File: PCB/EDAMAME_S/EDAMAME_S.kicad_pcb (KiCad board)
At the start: 2 copper layers, 80 x 87 mm, 62 parts, among them CN1 USB-B-MICRO, J1 Conn_01x20, J2 Conn_01x20, J5 Nichrome, M1 Motor_L, M2 Motor_R, Q1 2N7002DW, Q2 FDS4675, Q3 2SC2712, SW1 power, SW2 RST, U1 microSD, U2 FT231XS, U3 ESP32-WROOM, U4 TPS63000, U5 LSM303C, U6 GYSFDMAXB, U7 BD6211F, U8 INA226, U9 BD6211F

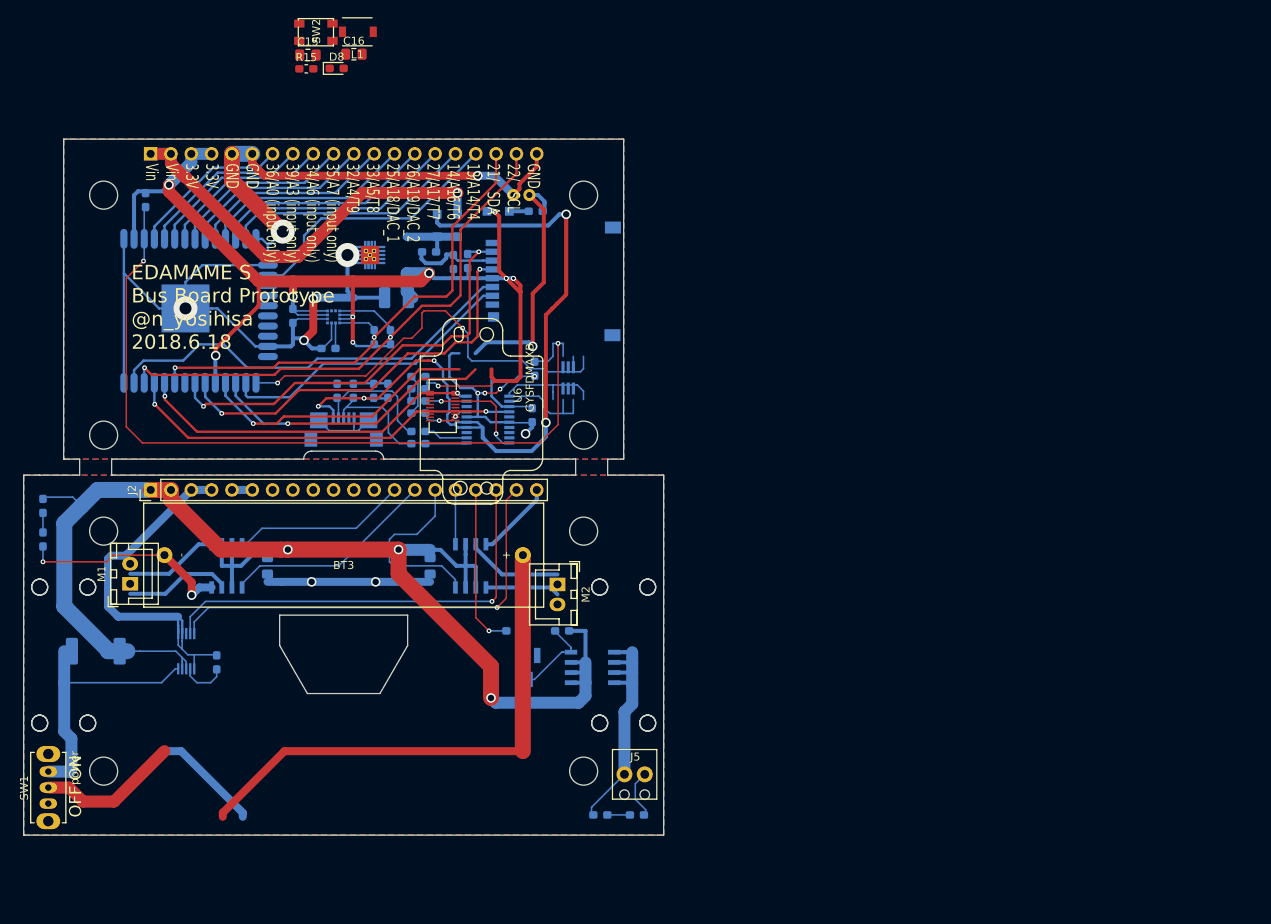
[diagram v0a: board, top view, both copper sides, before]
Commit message: AVR フットプリント・基板外形割当
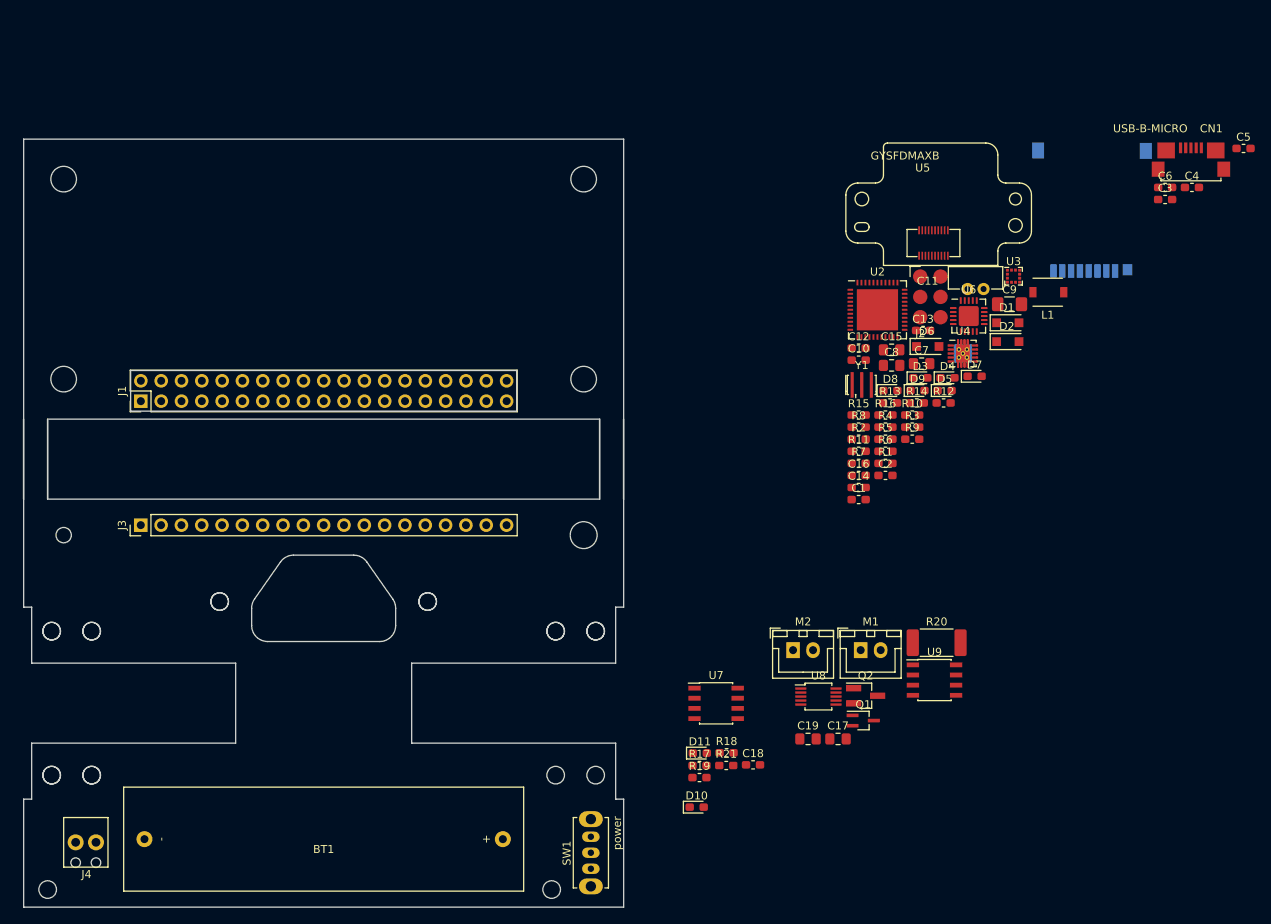
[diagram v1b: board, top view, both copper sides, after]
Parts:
- removed BT3: 10440, user:BH-411
- removed J5: Nichrome, user:MPT0.5_2-2.54
- removed Q3: 2SC2712, Package_TO_SOT_SMD:SOT-23_Handsoldering
- removed SW2: RST, user:SKRPACE010_kai
- added C17: 10u, Capacitor_SMD:C_0805_2012Metric_Pad1.15x1.40mm_HandSolder, F.Cu at (130.3, 92.1)
- added C18: 0.1u, Capacitor_SMD:C_0603_1608Metric_Pad1.05x0.95mm_HandSolder, F.Cu at (119.7, 95.4)
- added C19: 10u, Capacitor_SMD:C_0805_2012Metric_Pad1.15x1.40mm_HandSolder, F.Cu at (126.6, 92.1)
- added D10: Nichrome, LED_SMD:LED_0603_1608Metric_Pad1.05x0.95mm_HandSolder, F.Cu at (112.7, 100.7)
- added D11: POWER, LED_SMD:LED_0603_1608Metric_Pad1.05x0.95mm_HandSolder, F.Cu at (113.1, 93.9)
- added D9: RX_LED, LED_SMD:LED_0603_1608Metric_Pad1.05x0.95mm_HandSolder, F.Cu at (140.3, 48.6)
- added J3: Conn, Connector_PinHeader_2.54mm:PinHeader_1x19_P2.54mm_Vertical, F.Cu at (43.2, 65.4)
- added J4: Nichrome, user:MPT0.5_2-2.54, F.Cu at (33.6, 108.2)
- added R16: 1k, Resistor_SMD:R_0603_1608Metric_Pad1.05x0.95mm_HandSolder, F.Cu at (136.3, 51.6)
- added R17: 10K, Resistor_SMD:R_0603_1608Metric_Pad1.05x0.95mm_HandSolder, F.Cu at (113.0, 95.5)
- added R18: 1K, Resistor_SMD:R_0603_1608Metric_Pad1.05x0.95mm_HandSolder, F.Cu at (116.4, 93.9)
- added R19: 10K, Resistor_SMD:R_0603_1608Metric_Pad1.05x0.95mm_HandSolder, F.Cu at (113.0, 97.0)
- added R20: 10m, Resistor_SMD:R_2512_6332Metric_Pad1.52x3.35mm_HandSolder, F.Cu at (142.7, 80.1)
- added R21: 1K, Resistor_SMD:R_0603_1608Metric_Pad1.05x0.95mm_HandSolder, F.Cu at (116.4, 95.5)
- added Y1: 16MHz, Crystal:Resonator_SMD_muRata_CSTxExxV-3Pin_3.0x1.1mm_HandSoldering, F.Cu at (133.3, 47.9)
- BT1: value BACKUP -> 10440; footprint user:MS621FE_FL11E -> user:BH-411; moved to F.Cu
- C1, C12, C2, C5, CN1: moved to F.Cu
- C10: value 100u -> 0.1u; footprint Capacitor_SMD:C_1210_3225Metric_Pad1.42x2.65mm_HandSolder -> Capacitor_SMD:C_0603_1608Metric_Pad1.05x0.95mm_HandSolder; moved to F.Cu
- C11: value 10u -> 0.22F 3.3V; footprint Capacitor_SMD:C_0805_2012Metric_Pad1.15x1.40mm_HandSolder -> user:MS621FE_FL11E; moved to F.Cu
- C13: value 10u -> 47p; footprint Capacitor_SMD:C_0805_2012Metric_Pad1.15x1.40mm_HandSolder -> Capacitor_SMD:C_0603_1608Metric_Pad1.05x0.95mm_HandSolder; moved to F.Cu
- C14: value 0.1u -> 47p; moved to F.Cu
- C16: value 10u -> 0.1u; footprint Capacitor_SMD:C_0805_2012Metric_Pad1.15x1.40mm_HandSolder -> Capacitor_SMD:C_0603_1608Metric_Pad1.05x0.95mm_HandSolder
- C3, C4: value 47p -> 0.1u; moved to F.Cu
- C6: value 10u -> 0.1u; moved to F.Cu
- C7, C8: value 0.1u -> 10u; footprint Capacitor_SMD:C_0603_1608Metric_Pad1.05x0.95mm_HandSolder -> Capacitor_SMD:C_0805_2012Metric_Pad1.15x1.40mm_HandSolder; moved to F.Cu
- C9: value 0.1u -> 100u; footprint Capacitor_SMD:C_0603_1608Metric_Pad1.05x0.95mm_HandSolder -> Capacitor_SMD:C_1206_3216Metric_Pad1.42x1.75mm_HandSolder; moved to F.Cu
- D1: value TXLED -> GS1010FL; footprint LED_SMD:LED_0603_1608Metric_Pad1.05x0.95mm_HandSolder -> Diode_SMD:D_SOD-123F; moved to F.Cu
- D2: value RXLED -> GS1010FL; footprint LED_SMD:LED_0603_1608Metric_Pad1.05x0.95mm_HandSolder -> Diode_SMD:D_SOD-123F; moved to F.Cu
- D3: value GS1010FL -> POWER; footprint Diode_SMD:D_SOD-123F -> LED_SMD:LED_0603_1608Metric_Pad1.05x0.95mm_HandSolder; moved to F.Cu
- D4: value GS1010FL -> LED1; footprint Diode_SMD:D_SOD-123F -> LED_SMD:LED_0603_1608Metric_Pad1.05x0.95mm_HandSolder; moved to F.Cu
- D5: value GS1010FL -> LED2; footprint Diode_SMD:D_SOD-123F -> LED_SMD:LED_0603_1608Metric_Pad1.05x0.95mm_HandSolder; moved to F.Cu
- D6: value Nichrome -> GS1010FL; footprint LED_SMD:LED_0603_1608Metric_Pad1.05x0.95mm_HandSolder -> Diode_SMD:D_SOD-123F; moved to F.Cu
- D7: value POWER -> 1PPS; moved to F.Cu
- D8: value GPS -> TX_LED
- J1: value Conn_01x20 -> Conn; footprint Connector_PinHeader_2.54mm:PinHeader_1x20_P2.54mm_Vertical -> Connector_PinHeader_2.54mm:PinHeader_2x19_P2.54mm_Vertical; moved to F.Cu
- J2: value Conn_01x20 -> ISP; footprint Connector_PinHeader_2.54mm:PinHeader_1x20_P2.54mm_Vertical -> user:AVR_ISP
- L1: value 2.2uH VLF4012-2R2 -> 2.2uH
- Q1: value 2N7002DW -> MTM231102LBF; footprint Package_TO_SOT_SMD:SOT-363_SC-70-6_Handsoldering -> Package_TO_SOT_SMD:SOT-323_SC-70_Handsoldering; moved to F.Cu
- Q2: value FDS4675 -> 2SC2712; footprint Package_SO:SOIC-8_3.9x4.9mm_P1.27mm -> Package_TO_SOT_SMD:SOT-23_Handsoldering; moved to F.Cu
- R1: value 10K -> 10k; moved to F.Cu
- R10: value 1K -> 1k; moved to F.Cu
- R11: value 10K -> 100; moved to F.Cu
- R12: value 10m -> 1k; footprint Resistor_SMD:R_2512_6332Metric_Pad1.52x3.35mm_HandSolder -> Resistor_SMD:R_0603_1608Metric_Pad1.05x0.95mm_HandSolder; moved to F.Cu
- R13: value 1K -> 33; moved to F.Cu
- R14: value 10K -> 33; moved to F.Cu
- R15: value 1K -> 1k
- R2, R3: value 33 -> 10k; moved to F.Cu
- R4, R5: value 1K -> 10k; moved to F.Cu
- R6, R7: value 2.2K -> 2.2k; moved to F.Cu
- R8: value 100 -> 1k; moved to F.Cu
- R9: value 10K -> 1k; moved to F.Cu
- U2: value FT231XS -> ATMEGA1284P-MU; footprint user:FT231XS -> Package_DFN_QFN:QFN-44-1EP_7x7mm_P0.5mm_EP5.15x5.15mm; moved to F.Cu
- U3: value ESP32-WROOM -> LSM303C; footprint ESP32-footprints-Lib:ESP32-WROOM -> Package_LGA:LGA-12_2x2mm_P0.5mm; moved to F.Cu
- U4: value TPS63000 -> TPS63001; moved to F.Cu
- U5: value LSM303C -> GYSFDMAXB; footprint Housings_LGA:LGA-12_2x2mm_Pitch0.5mm -> user:GYSFDMAXB; moved to F.Cu
- U6: value GYSFDMAXB -> FT231XQ; footprint user:GYSFDMAXB -> Package_DFN_QFN:QFN-20-1EP_4x4mm_P0.5mm_EP2.5x2.5mm
- U7, U9: footprint Housings_SOIC:SOIC-8_3.9x4.9mm_Pitch1.27mm -> Package_SO:SOIC-8_3.9x4.9mm_P1.27mm; moved to F.Cu
- U8: footprint Housings_SSOP:MSOP-10_3x3mm_Pitch0.5mm -> Package_SO:MSOP-10_3x3mm_P0.5mm; moved to F.Cu
- moved D7 118.2 mm to (147.4, 46.8), turned to 0 degrees
- moved C5 112.9 mm to (181.0, 18.3), turned to 0 degrees
- moved CN1 111.2 mm to (174.5, 20.9), turned to 0 degrees
- moved R12 110.4 mm to (143.5, 50.1), turned to 0 degrees
- moved C4 109.8 mm to (174.6, 23.2), turned to 0 degrees
- moved R13 106.7 mm to (136.8, 50.1), turned to 0 degrees
- moved U3 106.0 mm to (152.3, 34.3), turned to 0 degrees
- moved C3 104.3 mm to (171.2, 24.7), turned to 0 degrees
- moved C6 100.4 mm to (171.2, 23.2), turned to 0 degrees
- moved J2 99.8 mm to (140.6, 34.3), turned to 0 degrees
- moved R14 99.7 mm to (140.2, 50.1), turned to 0 degrees
- moved L1 92.2 mm to (156.6, 36.3)
- moved M1 91.7 mm to (133.2, 81.0), turned to 0 degrees
- moved C12 89.3 mm to (132.9, 43.3), turned to 0 degrees
- moved C13 87.1 mm to (141.0, 41.1), turned to 0 degrees
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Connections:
- BT1 pad 2: GND -> GNDPWR
- C11 pad 1: +BATT -> Net-(C11-Pad1)
- C11 pad 2: GNDPWR -> GND
- C12 pad 1: VCC -> Net-(C12-Pad1)
- C12 pad 2: GNDPWR -> /EDAMAME_S_core/RST
- C13 pad 1: +BATT -> Net-(C13-Pad1)
- C13 pad 2: GNDPWR -> GND
- C14 pad 1: /EN -> Net-(C13-Pad1)
- C15 pad 1: Net-(C15-Pad1) -> +5V
- C16 pad 1: +3V3 -> +5V
- C3 pad 1: Net-(C3-Pad1) -> +3V3
- C4 pad 1: Net-(C4-Pad1) -> +3V3
- C5 pad 1: +5V -> +3V3
- C6 pad 1: +5V -> Net-(C6-Pad1)
- C7 pad 1: +3V3 -> Net-(C7-Pad1)
- C8 pad 1: Net-(C8-Pad1) -> +3V3
- C9 pad 1: Net-(C15-Pad1) -> +3V3
- CN1 pad 2: Net-(C4-Pad1) -> Net-(C13-Pad1)
- CN1 pad 3: Net-(C3-Pad1) -> Net-(CN1-Pad3)
- D1 pad 1: Net-(D1-Pad1) -> Net-(C7-Pad1)
- D2 pad 1: Net-(D2-Pad1) -> Net-(C7-Pad1)
- D2 pad 2: Net-(D2-Pad2) -> +5V
- D3 pad 1: Net-(C15-Pad1) -> GND
- D3 pad 2: +5V -> Net-(D3-Pad2)
- D4 pad 1: Net-(C15-Pad1) -> GND
- D4 pad 2: VDC -> Net-(D4-Pad2)
- D5 pad 1: Net-(D5-Pad1) -> GND
- D5 pad 2: +3V3 -> Net-(D5-Pad2)
- D6 pad 1: GNDPWR -> Net-(C11-Pad1)
- D7 pad 1: GNDPWR -> GND
- D8 pad 1: GND -> Net-(D8-Pad1)
- J1 pad 1: VDC -> Net-(J1-Pad1)
- J1 pad 10: /IO35 -> /EDAMAME_S_core/18
- J1 pad 11: /IO32 -> /EDAMAME_S_core/1
- J1 pad 12: /IO33 -> /EDAMAME_S_core/19
- J1 pad 13: /IO25 -> /EDAMAME_S_core/2
- J1 pad 14: /IO26 -> /EDAMAME_S_core/20
- J1 pad 15: /IO27 -> /EDAMAME_S_core/3-
- J1 pad 16: /IO14 -> /EDAMAME_S_core/21
- J1 pad 17: /IO13 -> /EDAMAME_S_core/PC→AVR
- J1 pad 18: /I2C_SDA -> /EDAMAME_S_core/22
- J1 pad 19: /I2C_SCL -> /EDAMAME_S_core/AVR→PC
- J1 pad 2: VDC -> Net-(D1-Pad2)
- J1 pad 20: GND -> /EDAMAME_S_core/23
- J1 pad 3: +3V3 -> Net-(J1-Pad1)
- J1 pad 4: +3V3 -> Net-(D1-Pad2)
- J1 pad 5: GND -> +3V3
- J1 pad 6: GND -> +3V3
- J1 pad 7: /S_VP -> GND
- J1 pad 8: /S_VN -> GND
- J1 pad 9: /IO34 -> /EDAMAME_S_core/0
- J2 pad 1: +BATT -> /EDAMAME_S_core/MISO
- J2 pad 2: +BATT -> +3V3
- J2 pad 3: VCC -> /EDAMAME_S_core/SCK
- J2 pad 4: VCC -> /EDAMAME_S_core/MOSI
- J2 pad 5: GNDPWR -> /EDAMAME_S_core/RST
- J2 pad 6: GNDPWR -> GND
- Q1 pad 1: /RST -> Net-(Q1-Pad1)
- Q1 pad 2: /DTR -> Net-(J4-Pad1)
- Q1 pad 3: /BOOT -> +BATT
- Q2 pad 1: +BATT -> Net-(Q2-Pad1)
- Q2 pad 2: +BATT -> GNDPWR
- Q2 pad 3: +BATT -> Net-(Q1-Pad1)
- R1 pad 1: +3V3 -> /EDAMAME_S_core/SS
- R1 pad 2: /SPI_MISO -> +3V3
- R10 pad 1: Net-(J5-Pad1) -> /EDAMAME_S_core/18
- R10 pad 2: Net-(D6-Pad2) -> Net-(D5-Pad2)
- R11 pad 1: Net-(Q3-Pad1) -> +3V3
- R11 pad 2: /Nichrome -> Net-(D6-Pad2)
- R12 pad 1: +BATT -> Net-(D7-Pad2)
- R13 pad 1: +BATT -> Net-(R13-Pad1)
- R13 pad 2: Net-(D7-Pad2) -> Net-(C13-Pad1)
- R14 pad 1: /EN -> Net-(R14-Pad1)
- R14 pad 2: +3V3 -> Net-(CN1-Pad3)
- R15 pad 1: Net-(R15-Pad1) -> +3V3
- R2 pad 1: Net-(R2-Pad1) -> /EDAMAME_S_core/MOSI
- R2 pad 2: Net-(C4-Pad1) -> +3V3
- R3 pad 1: Net-(R3-Pad1) -> /EDAMAME_S_core/SCK
- R3 pad 2: Net-(C3-Pad1) -> +3V3
- R4 pad 1: +3V3 -> /EDAMAME_S_core/MISO
- R4 pad 2: Net-(D1-Pad2) -> +3V3
- R5 pad 2: Net-(D2-Pad2) -> /EDAMAME_S_core/RST
- R6 pad 1: /I2C_SDA -> +3V3
- R6 pad 2: +3V3 -> /EDAMAME_S_core/I2C_SDA
- R7 pad 1: /I2C_SCL -> +3V3
- R7 pad 2: +3V3 -> /EDAMAME_S_core/I2C_SCL
- R8 pad 1: Net-(BT1-Pad1) -> Net-(D3-Pad2)
- R8 pad 2: Net-(D5-Pad1) -> +3V3
- R9 pad 1: Net-(Q2-Pad4) -> /EDAMAME_S_core/19
- R9 pad 2: +BATT -> Net-(D4-Pad2)
- SW1 pad 1: Net-(R12-Pad2) -> Net-(R20-Pad2)
- SW1 pad 2: Net-(BT3-Pad1) -> Net-(BT1-Pad1)
- U1 pad 2: /SPI_CS -> /EDAMAME_S_core/SS
- U1 pad 3: /SPI_MOSI -> /EDAMAME_S_core/MOSI
- U1 pad 5: /SPI_SCLK -> /EDAMAME_S_core/SCK
- U1 pad 7: /SPI_MISO -> /EDAMAME_S_core/MISO
- U2 pad 1: /DTR -> /EDAMAME_S_core/MOSI
- U2 pad 10: Net-(D2-Pad1) -> /EDAMAME_S_core/AVR→PC
- U2 pad 11: Net-(R3-Pad1) -> /EDAMAME_S_core/GPS→AVR
- U2 pad 12: Net-(R2-Pad1) -> /EDAMAME_S_core/AVR→GPS
- U2 pad 13: Net-(U2-Pad13) -> /EDAMAME_S_core/12-
- U2 pad 14: +5V -> /EDAMAME_S_core/13-
- U2 pad 15: +5V -> /EDAMAME_S_core/14-
- U2 pad 16: GND -> /EDAMAME_S_core/15-
- U2 pad 17: Net-(D1-Pad1) -> +3V3
- U2 pad 18: Net-(U2-Pad18) -> GND
- U2 pad 19: Net-(U2-Pad19) -> /EDAMAME_S_core/I2C_SCL
- U2 pad 2: /RST -> /EDAMAME_S_core/MISO
- U2 pad 20: /PC→ESP32 -> /EDAMAME_S_core/I2C_SDA
- U2 pad 3: +3V3 -> /EDAMAME_S_core/SCK
- U2 pad 4: /ESP32→PC -> /EDAMAME_S_core/RST
- U2 pad 5: Net-(U2-Pad5) -> +3V3
- U2 pad 9: Net-(U2-Pad9) -> /EDAMAME_S_core/PC→AVR
- U3 pad 1: GND -> /EDAMAME_S_core/I2C_SCL
- U3 pad 10: /IO25 -> +3V3
- U3 pad 11: /IO26 -> Net-(U3-Pad11)
- U3 pad 12: /IO27 -> Net-(U3-Pad12)
- U3 pad 2: Net-(U3-Pad2) -> +3V3
- U3 pad 3: /EN -> +3V3
- U3 pad 4: /S_VP -> /EDAMAME_S_core/I2C_SDA
- U3 pad 5: /S_VN -> Net-(C6-Pad1)
- U3 pad 6: /IO34 -> GND
- U3 pad 7: /IO35 -> Net-(U3-Pad7)
- U3 pad 8: /IO32 -> GND
- U3 pad 9: /IO33 -> +3V3
- U4 pad 11: (no net) -> GND
- U4 pad 5: Net-(C15-Pad1) -> Net-(C7-Pad1)
- U4 pad 6: Net-(C15-Pad1) -> Net-(C7-Pad1)
- U4 pad 7: Net-(C15-Pad1) -> Net-(C7-Pad1)
- U4 pad 8: Net-(C15-Pad1) -> Net-(C7-Pad1)
- U5 pad 1: /I2C_SCL -> GND
- U5 pad 10: +3V3 -> GND
- U5 pad 11: Net-(U5-Pad11) -> (no net)
- U5 pad 12: Net-(U5-Pad12) -> GND
- U5 pad 2: +3V3 -> GND
- U5 pad 3: +3V3 -> /EDAMAME_S_core/AVR→GPS
- U5 pad 4: /I2C_SDA -> Net-(U5-Pad4)
- U5 pad 5: Net-(C8-Pad1) -> /EDAMAME_S_core/GPS→AVR
- U5 pad 6: GND -> Net-(R12-Pad2)
- U5 pad 7: Net-(U5-Pad7) -> GND
- U5 pad 8: GND -> (no net)
- U5 pad 9: +3V3 -> (no net)
- U6 pad 1: GND -> /EDAMAME_S_core/AVR→PC
- U6 pad 10: GND -> Net-(U6-Pad10)
- U6 pad 11: Net-(U6-Pad11) -> +5V
- U6 pad 12: GND -> +5V
- U6 pad 13: Net-(U6-Pad13) -> GND
- U6 pad 14: Net-(BT1-Pad1) -> Net-(D9-Pad1)
- U6 pad 15: Net-(U6-Pad15) -> Net-(D8-Pad1)
- U6 pad 16: +3V3 -> Net-(U6-Pad16)
- U6 pad 17: Net-(U6-Pad17) -> /EDAMAME_S_core/PC→AVR
- U6 pad 18: Net-(U6-Pad18) -> Net-(C12-Pad1)
- U6 pad 19: GND -> Net-(U6-Pad19)
- U6 pad 2: GND -> Net-(U6-Pad2)
- U6 pad 20: GND -> +3V3
- U6 pad 3: /ESP32→GPS -> GND
- U6 pad 5: /GPS→ESP32 -> Net-(U6-Pad5)
- U6 pad 6: Net-(R15-Pad1) -> Net-(U6-Pad6)
- U6 pad 7: GND -> Net-(U6-Pad7)
- U6 pad 8: Net-(U6-Pad8) -> Net-(R14-Pad1)
- U6 pad 9: Net-(U6-Pad9) -> Net-(R13-Pad1)
- U7 pad 4: /MOTOR_LF -> /EDAMAME_S_Ex/MOTOR_LF
- U7 pad 5: /MOTOR_LR -> /EDAMAME_S_Ex/MOTOR_LR
- U8 pad 10: Net-(R12-Pad2) -> Net-(R20-Pad2)
- U8 pad 4: /SDA -> /EDAMAME_S_Ex/SDA
- U8 pad 5: /SCL -> /EDAMAME_S_Ex/SCL
- U9 pad 4: /MOTOR_RR -> /EDAMAME_S_Ex/MOTOR_RR
- U9 pad 5: /MOTOR_RF -> /EDAMAME_S_Ex/MOTOR_RF
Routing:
- net GND: track 212.6 -> 0.00 mm, vias 11 -> 0
- net +BATT: track 172.9 -> 0.00 mm, vias 3 -> 0
- net +3V3: track 169.3 -> 0.00 mm, vias 12 -> 0
- net /EN: track 101.2 -> 0.00 mm, vias 2 -> 0
- net +5V: track 97.7 -> 0.00 mm, vias 5 -> 0
- net Net-(BT3-Pad1): track 83.6 -> 0.00 mm
- net /I2C_SCL: track 74.9 -> 0.00 mm, vias 2 -> 0
- net GNDPWR: track 71.1 -> 0.00 mm, vias 4 -> 0
- net /I2C_SDA: track 66.1 -> 0.00 mm, vias 2 -> 0
- net /SCL: track 55.8 -> 0.00 mm, vias 1 -> 0
- net /SDA: track 54.8 -> 0.00 mm, vias 1 -> 0
- net /BOOT: track 54.3 -> 0.00 mm, vias 2 -> 0
- net /SPI_MISO: track 54.3 -> 0.00 mm, vias 2 -> 0
- net /SPI_MOSI: track 53.1 -> 0.00 mm
- net /SPI_SCLK: track 50.8 -> 0.00 mm, vias 2 -> 0
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- removed copper zone on B.Cu, net GND
- removed copper zone on F.Cu, net GND
- removed copper zone on B.Cu, net GNDPWR
- removed copper zone on F.Cu, net GNDPWR
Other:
- board size 80 x 87 mm -> 75 x 96 mm
- board text removed: "+ -"
- board text removed: "@n_yosihisa 2018.6.18 EDAMAME S Extension Board"
- board text removed: "EDAMAME S Bus Board Prototype @n_yosihisa 2018.6.18"
- board text removed: "GND 22/ SCL 21/ SDA 13/A14/T4 14/A16/T6 27/A17/T7 26/A19/DAC_2 25/A18/DAC_1 33/A5/T8 32/A4/T9 35/A7 (input only) 34/A6 (input only) 39/A3 (input only) 36/A0 (input only) GND GND 3.3V 3.3V Vin Vin"
- board text removed: "OFF ON"
